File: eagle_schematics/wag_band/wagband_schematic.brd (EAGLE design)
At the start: 100 x 80 mm, 14 parts, among them U2 TLV1117-33CDCY

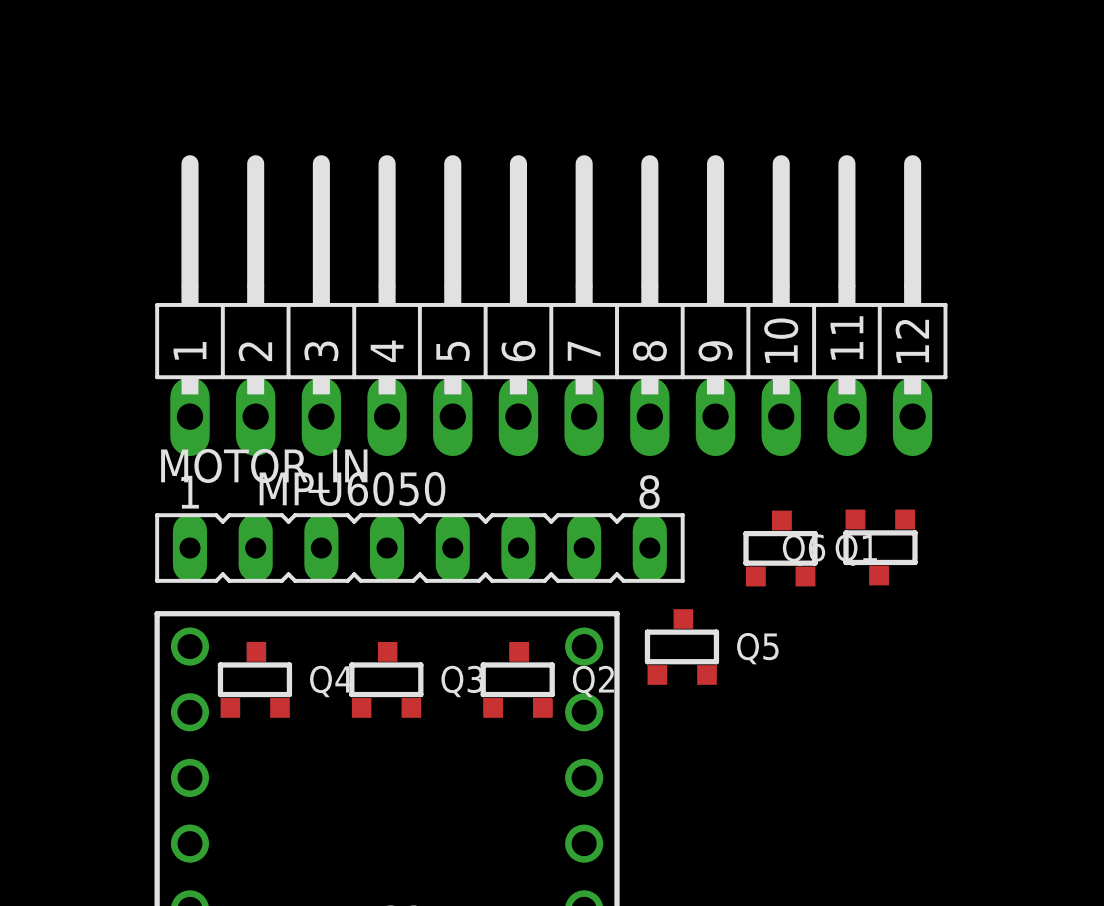
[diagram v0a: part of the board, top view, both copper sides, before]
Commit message: Adding updated schematics and some sample code for Matt testing motors
Straight up chillin
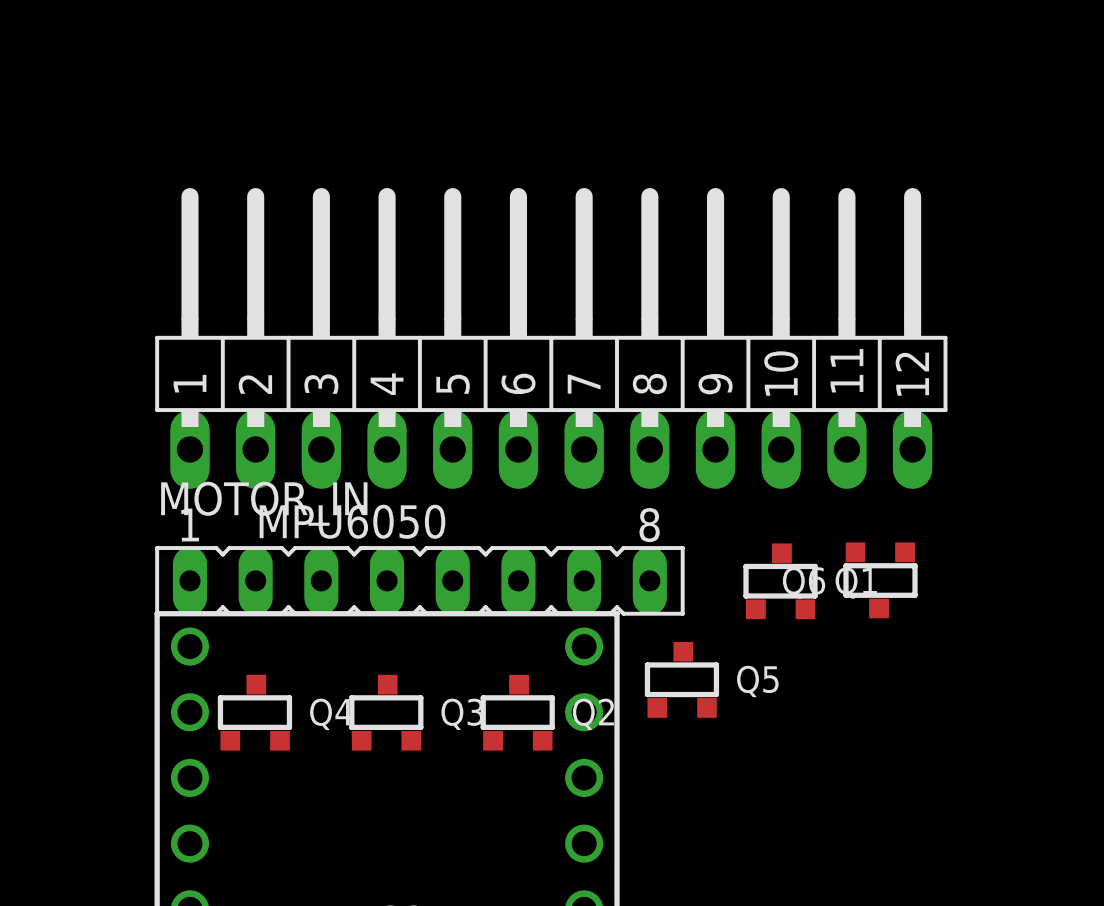
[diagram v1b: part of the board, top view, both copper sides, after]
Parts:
- moved MOTOR_IN 1.27 mm to (30.5, 54.6)
- moved Q5 1.27 mm to (35.6, 45.7)
- moved MPU6050 1.27 mm to (25.4, 49.5)
- moved Q1 1.27 mm to (39.4, 49.5)
- moved Q2 1.27 mm to (29.2, 44.5)
- moved Q3 1.27 mm to (24.1, 44.5)
- moved Q4 1.27 mm to (19.1, 44.5)
- moved Q6 1.27 mm to (43.2, 49.5)

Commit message: Added more parts for eagle
Finished PCBs
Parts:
- removed BATTERY: (no value), adafruit:JST-PH-2-THM-RA
- removed ESP8266_HDR: (no value), pinhead:2X04
- removed MPU6050: (no value), con-lsta:FE08
- added BAT, CHGR: (no value), adafruit:JST-PH-2-THM-RA
- added JP1: (no value), mqp_custom_parts:MPU6050
- added LED1, PWR: (no value), led:LED5MM
- added Q7, Q8: (no value), mqp_custom_parts:SOT-23
- added R1, R5: 1k, resistor:R1206
- added R2, R3: 30k, resistor:R1206
- added R4: 10k, resistor:R1206
- added U$2: ESP01, esp8266modules:ESP01
- added U$3: CB10LV103M, mqp_custom_parts:CB10
- added U$4: MS12ASW13, mqp_custom_parts:SPDT
- added U1: LM358DR, Texas Instruments_By_element14_Batch_1:SOIC127P600X175-8N
- C1, C2: device rcl:C025-024X044 -> resistor:C0805K
- moved C2 35.2 mm to (10.2, 2.54)
- moved U2 25.4 mm to (10.2, 7.62), turned to 180 degrees
- moved Q5 23.5 mm to (13.3, 53.3)
- moved Q6 23.2 mm to (20.3, 53.3), turned to 0 degrees
- moved Q1 22.5 mm to (17.1, 53.3)
- moved Q2 21.6 mm to (9.53, 53.3)
- moved Q3 19.9 mm to (6.35, 53.3)
- moved U$1 19.8 mm to (8.89, 17.8)
- moved C1 18.3 mm to (10.2, 12.7)
- moved Q4 18.2 mm to (3.17, 53.3)
- moved MOTOR_IN 13.0 mm to (17.8, 57.1)
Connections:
- removed net AGND: U$1.AGND
- new net N$12: U$1.8, U$2.RX
- new net N$18: U$1.11, U$2.GPIO2
- new net N$20: Q7.3, R1.1, U1.3
- new net N$22: LED1.K, R1.2
- new net N$23: Q7.1, Q8.3, R2.1
- new net N$24: R4.2, U$1.9, U$2.CH_PD
- new net N$25: Q8.1, U$3.P$3, U1.2
- new net N$26: U$1.12, U1.1
- new net N$27: R3.1, U$3.P$2
- new net N$28: BAT.1, U$4.P$2
- new net N$29: CHGR.1, U$4.P$1
- net GND: now also BAT.2, CHGR.2, JP1.GND, Q7.2, Q8.2, R5.1, U$1.AGND, U$2.GND, U$3.P$1, U1.4; no longer BATTERY.1, ESP8266_HDR.2, MPU6050.2
- net N$1: now also U$1.23/A9; no longer U$1.21/A7
- net N$17: now also JP1.SCL; no longer MPU6050.3
- net N$19: now also U$1.10, U$2.GPIO0; no longer ESP8266_HDR.8, U$1.1
- net N$21: now also PWR.K, R5.2; no longer ESP8266_HDR.5, U$1.7
- net N$3: now also U$1.22/A8; no longer U$1.20/A6
- net N$4: now also JP1.SDA; no longer MPU6050.4
- net N$7: now also U$1.7, U$2.TX; no longer ESP8266_HDR.1, U$1.0
- net N$8: now also JP1.INT; no longer MPU6050.8
- net VCC: now also JP1.VCC, LED1.A, PWR.A, R2.2, R3.2, R4.1, U$2.RST, U$2.VCC, U$4.P$3, U1.8; no longer BATTERY.2, ESP8266_HDR.3, ESP8266_HDR.7, MPU6050.1
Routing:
- net VCC: track 0.00 -> 205.0 mm, vias 0 -> 1
- net GND: track 0.00 -> 185.1 mm, vias 0 -> 1
- net N$2: track 0.00 -> 81.8 mm
- net N$1: track 0.00 -> 67.3 mm, vias 0 -> 1
- net N$5: track 0.00 -> 56.6 mm, vias 0 -> 1
- net N$20: track 0.00 -> 55.9 mm, vias 0 -> 3
- net N$3: track 0.00 -> 44.3 mm, vias 0 -> 2
- net N$16: track 0.00 -> 43.1 mm, vias 0 -> 1
- net N$25: track 0.00 -> 42.9 mm
- net N$6: track 0.00 -> 40.3 mm, vias 0 -> 1
- net N$28: track 0.00 -> 36.1 mm, vias 0 -> 1
- net N$8: track 0.00 -> 31.8 mm
- net N$26: track 0.00 -> 27.3 mm
- net N$17: track 0.00 -> 21.1 mm
- net N$4: track 0.00 -> 20.2 mm
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- added copper zone on layer 1, net GND
- added copper zone on layer 16, net GND
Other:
- board size 100 x 80 mm -> 34.3 x 63.5 mm
- board text added: "BAT"
- board text added: "CHGR"
- board text added: "POT"
- board text added: "Record. Play. Learn."
- board text added: "Team Suit Up!"
- board text added: "WAG Band Chas Frick Team Suit Up!"

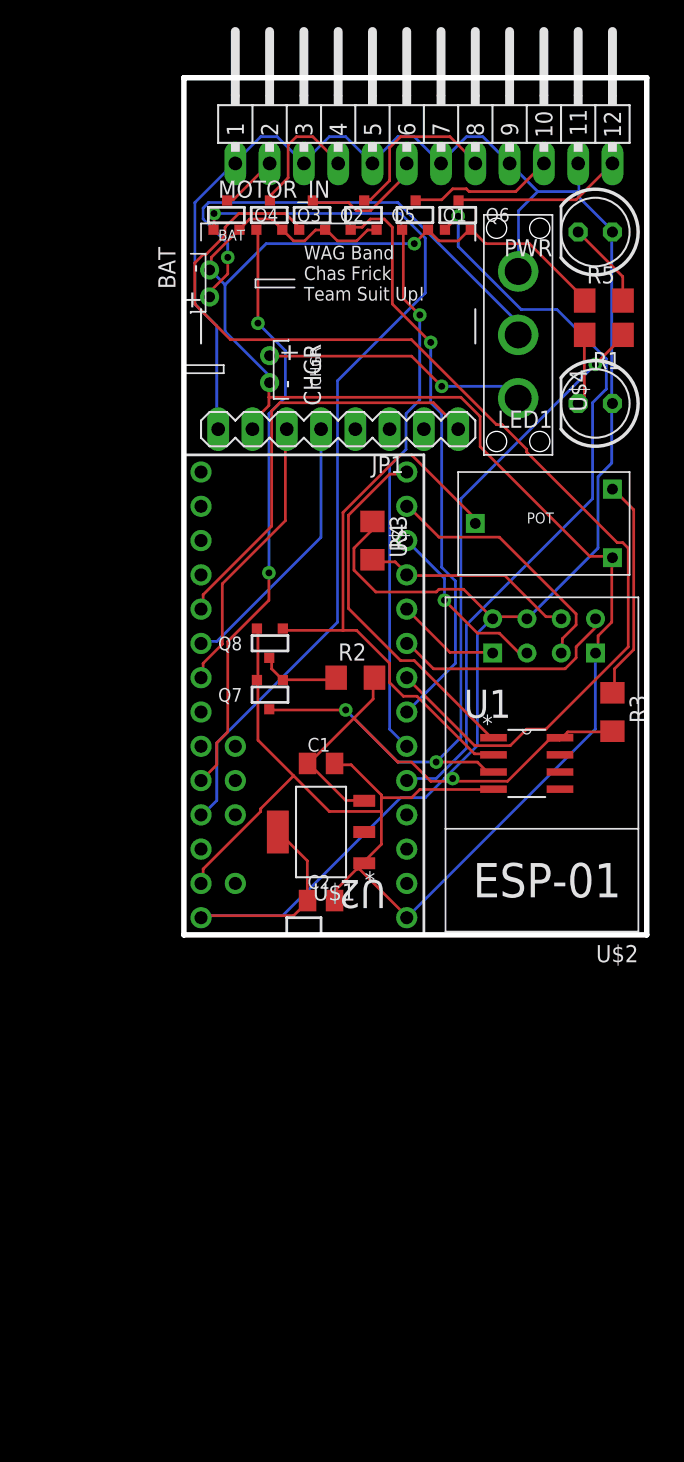
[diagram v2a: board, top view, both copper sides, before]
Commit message: Fixed all schematics and boards to have separate power supplies finally :100:
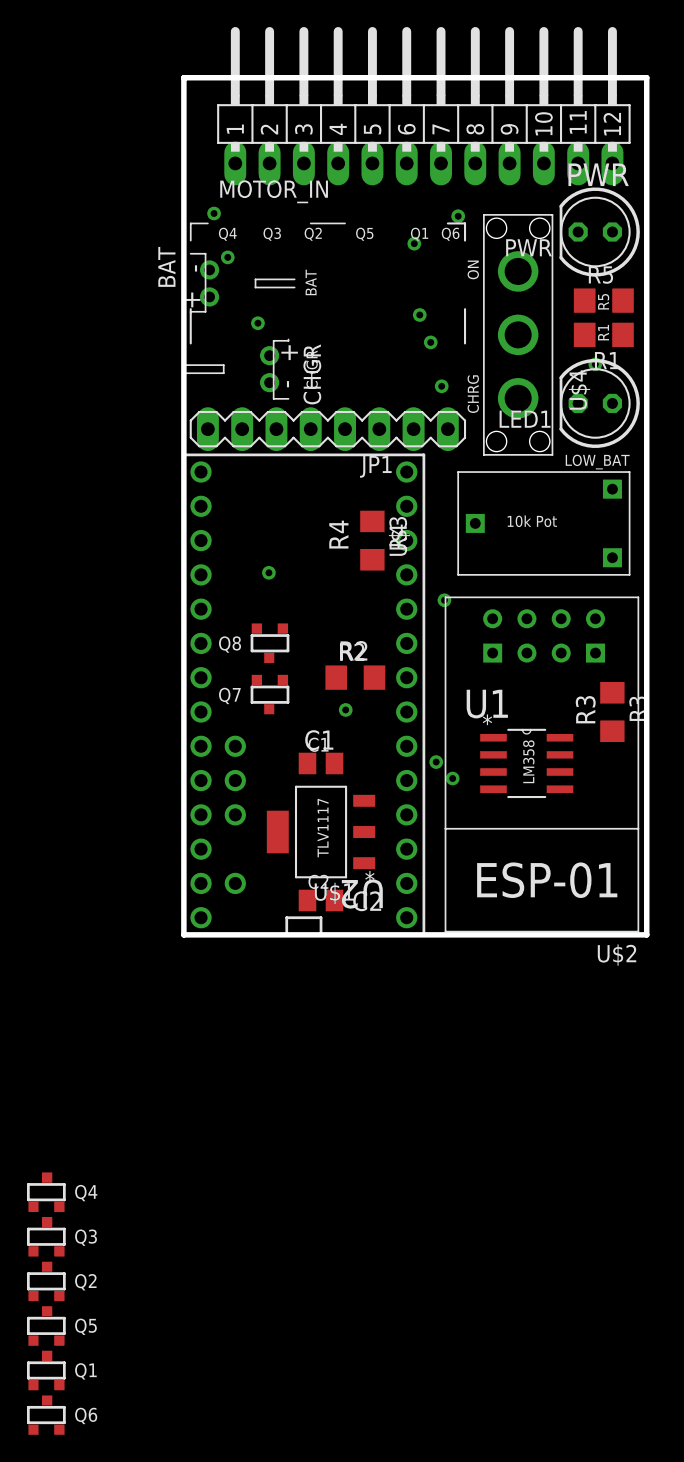
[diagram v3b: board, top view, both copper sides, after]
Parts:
- Q1, Q2, Q3, Q4, Q5, Q6: device transistors:SOT-23 -> mqp_custom_parts:SOT-23
- moved Q6 94.0 mm to (-10.2, -35.6)
- moved Q1 89.8 mm to (-10.2, -32.3)
- moved Q5 85.6 mm to (-10.2, -29.0)
- moved Q2 81.4 mm to (-10.2, -25.7)
- moved Q3 77.5 mm to (-10.2, -22.4)
- moved Q4 73.6 mm to (-10.2, -19.1)
- moved JP1 0.76 mm to (10.7, 37.5)
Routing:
- net VCC: track 205.0 -> 0.00 mm
- net GND: track 185.1 -> 0.00 mm
- net N$2: track 81.8 -> 0.00 mm
- net N$1: track 67.3 -> 0.00 mm
- net N$5: track 56.6 -> 0.00 mm
- net N$20: track 55.9 -> 0.00 mm
- net N$3: track 44.3 -> 0.00 mm
- net N$16: track 43.1 -> 0.00 mm
- net N$25: track 42.9 -> 0.00 mm
- net N$6: track 40.3 -> 0.00 mm
- net N$28: track 36.1 -> 0.00 mm
- net N$8: track 31.8 -> 0.00 mm
- net N$26: track 27.3 -> 0.00 mm
- net N$17: track 21.1 -> 0.00 mm
- net N$4: track 20.2 -> 0.00 mm
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- removed copper zone on layer 1, net GND
- removed copper zone on layer 16, net GND
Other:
- board text added: "10k Pot"
- board text added: "C1"
- board text added: "C2"
- board text added: "CHRG"
- board text added: "LM358"
- board text added: "LOW_BAT"
- board text added: "ON"
- board text added: "PWR"
- board text added: "Q1"
- board text added: "Q2"
- board text added: "Q3"
- board text added: "Q4"
- board text added: "Q5"
- board text added: "Q6"
- board text added: "R1"
- board text added: "R2"
- board text added: "R3"
- board text added: "R4"
- board text added: "R5"
- board text added: "TLV1117"
- board text removed: "POT"
- board text removed: "Team Suit Up!"
